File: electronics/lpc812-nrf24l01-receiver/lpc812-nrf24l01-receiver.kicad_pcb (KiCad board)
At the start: 2 copper layers, 25 x 24 mm, 21 parts, among them K1 BAT, K2 CH3, K3 TH, K4 ST, P1 NRF24L01+, SW1 ISP/BIND, U1 MCP1703T-3302E/CB, U2 LPC812M101JDH16_TSSOP16, X1 12 MHz

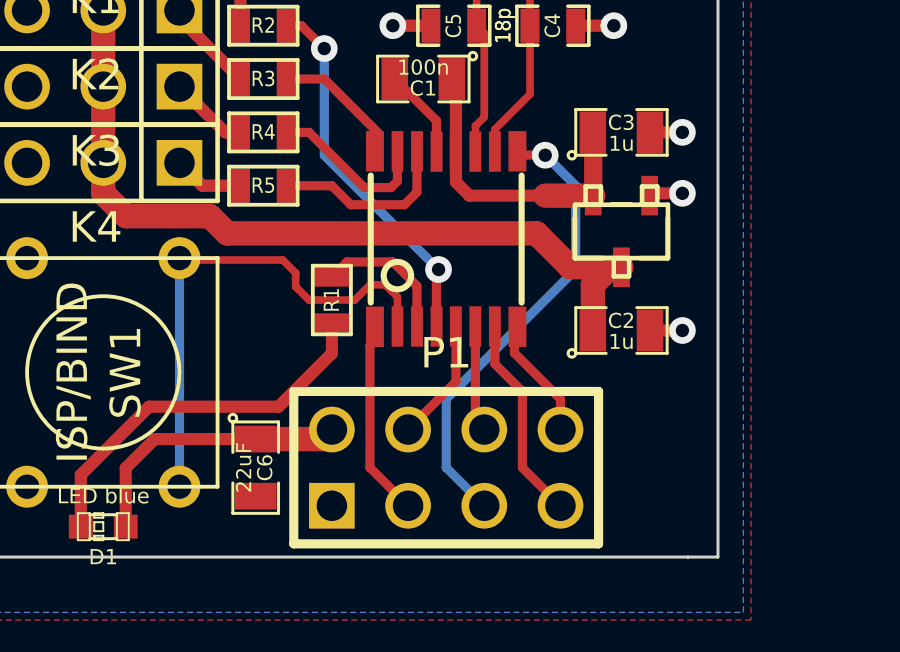
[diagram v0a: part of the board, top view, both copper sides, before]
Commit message: Make labels local
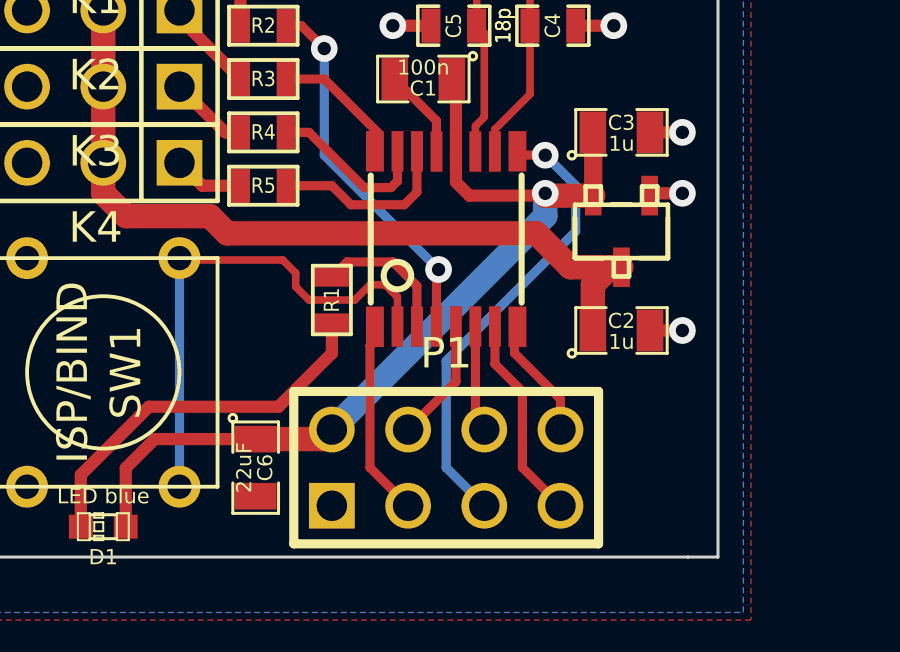
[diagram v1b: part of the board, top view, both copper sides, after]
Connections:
- net CE renamed /CE
- net CH1 renamed /CH1
- net CH2 renamed /CH2
- net CH3/Rx renamed /CH3/Rx
- net CH4/CPPM/Tx renamed /CPPM/Tx
- net CSN renamed /CSN
- net IRQ renamed /IRQ
- net ISP/BIND renamed /ISP/BIND
- net LED renamed /LED
- net MISO renamed /MISO
- net MOSI renamed /MOSI
- net SCK renamed /SCK
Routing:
- net +3.3V: track 20.0 -> 30.9 mm, vias 0 -> 1

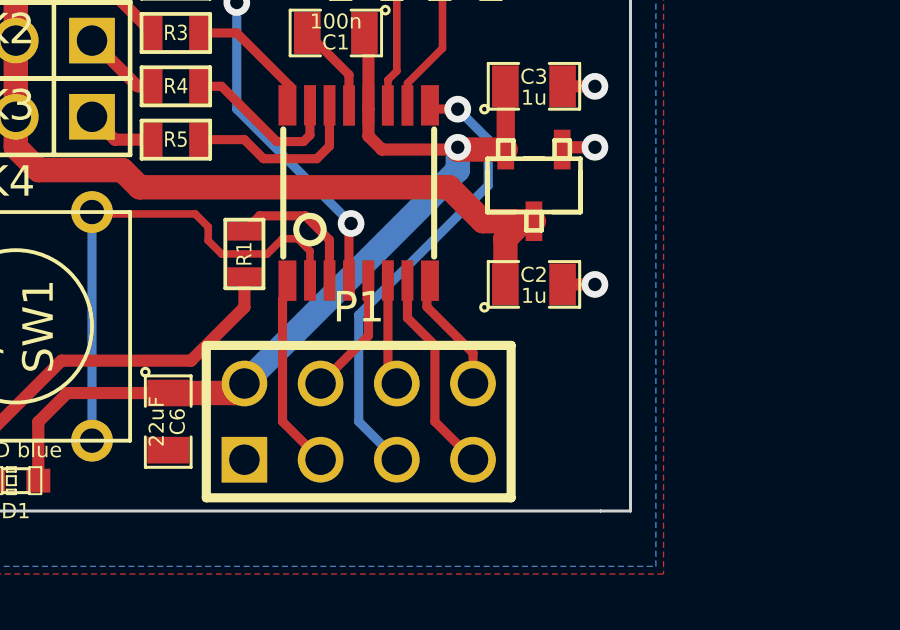
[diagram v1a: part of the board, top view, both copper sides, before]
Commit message: Tweak label names
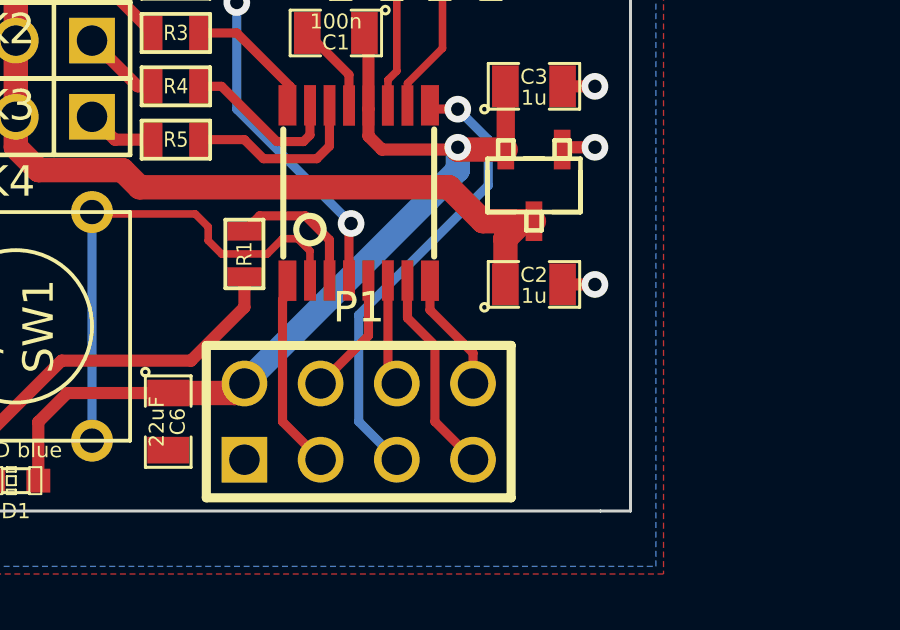
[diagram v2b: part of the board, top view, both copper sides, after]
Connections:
- net /CH3/Rx renamed /CH3-Rx
- net /CPPM/Tx renamed /Tx
- net /ISP/BIND renamed /ISP-BIND
- net N-0000021 renamed /XTALOUT
- net N-0000022 renamed /XTALIN

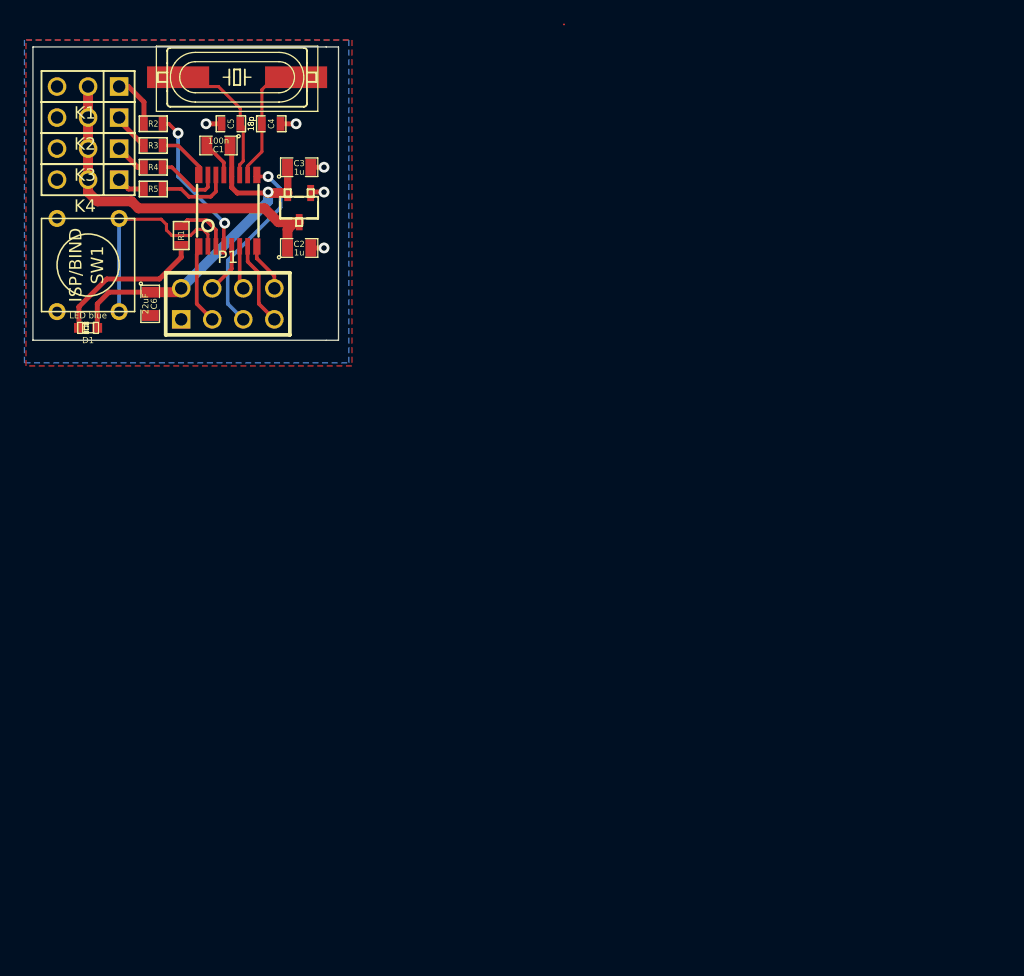
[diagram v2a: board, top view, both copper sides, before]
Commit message: Use new component libraries
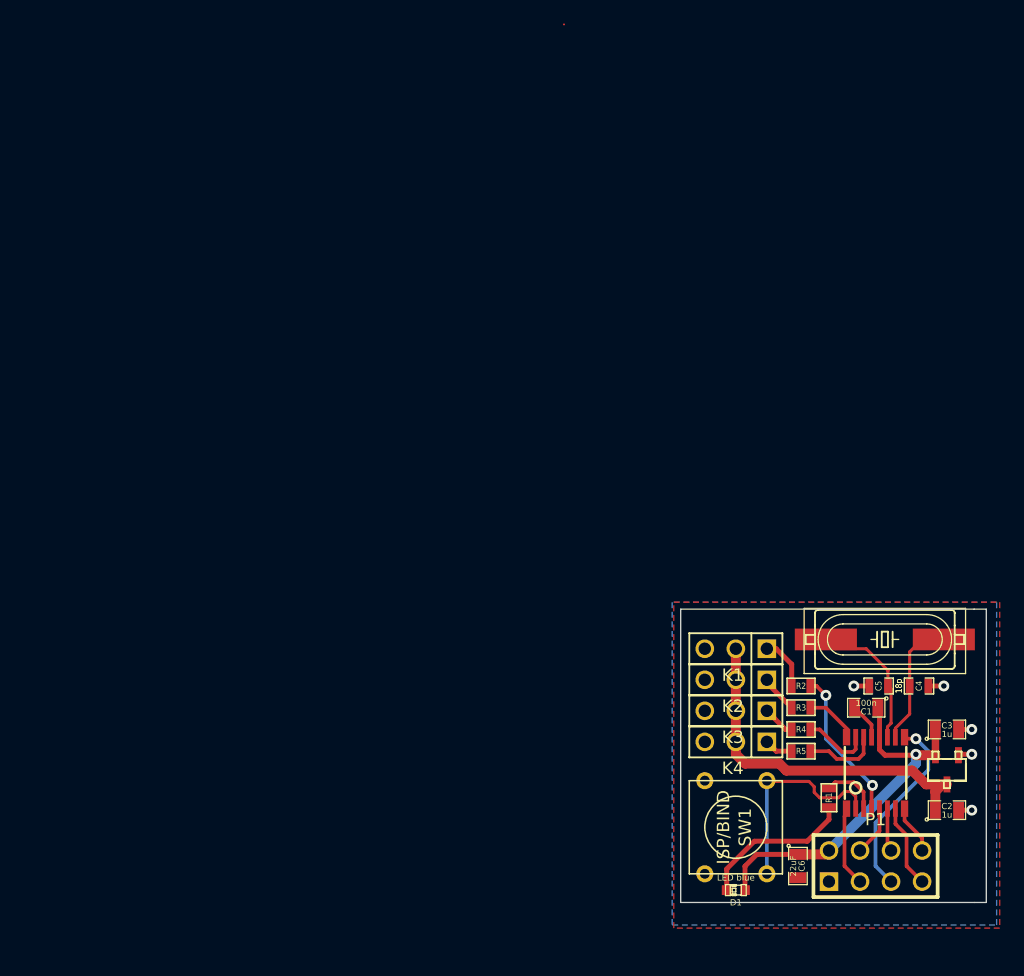
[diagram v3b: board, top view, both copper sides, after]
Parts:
- moved U2 70.2 mm to (80.9, 71.4)
- moved C1 70.2 mm to (80.2, 66.1)
- moved C2 70.2 mm to (86.8, 74.4)
- moved C3 70.2 mm to (86.8, 67.8)
- moved C4 70.2 mm to (84.5, 64.3)
- moved C5 70.2 mm to (81.2, 64.3)
- moved C6 70.2 mm to (74.6, 79.0)
- moved D1 70.2 mm to (69.5, 81.0)
- moved K1 70.2 mm to (69.5, 61.2)
- moved K2 70.2 mm to (69.5, 63.8)
- moved K3 70.2 mm to (69.5, 66.3)
- moved K4 70.2 mm to (69.5, 68.9)
- moved P1 70.2 mm to (80.9, 79.0)
- moved R1 70.2 mm to (77.1, 73.4)
- moved R2 70.2 mm to (74.8, 64.3)
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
